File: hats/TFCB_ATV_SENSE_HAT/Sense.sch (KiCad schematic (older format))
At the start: 0 parts

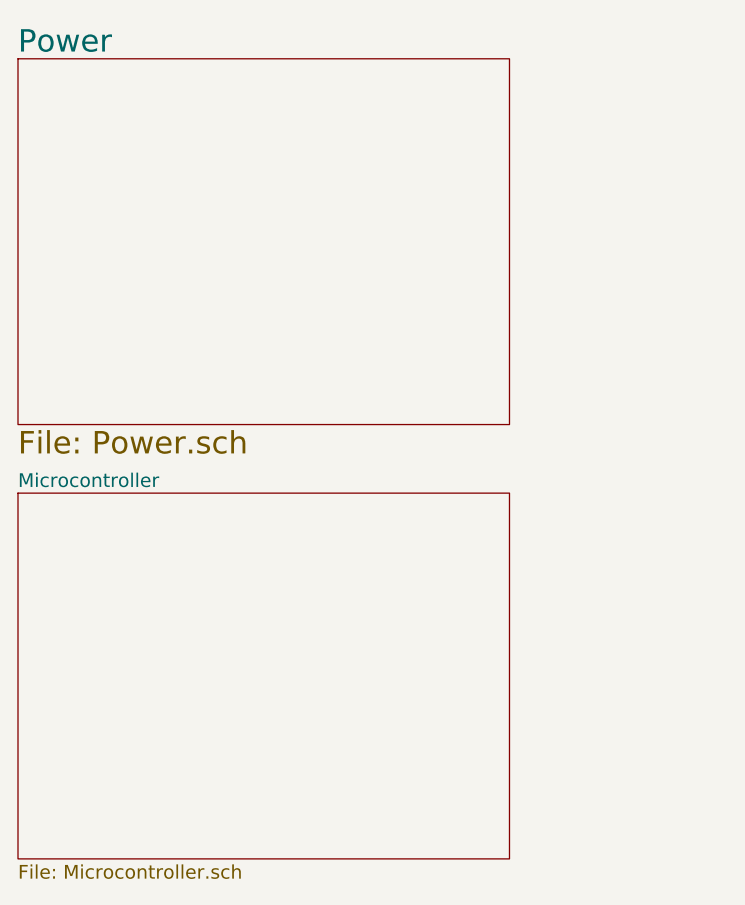
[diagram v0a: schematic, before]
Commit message: Moved power regulators to top side and corrected bad package
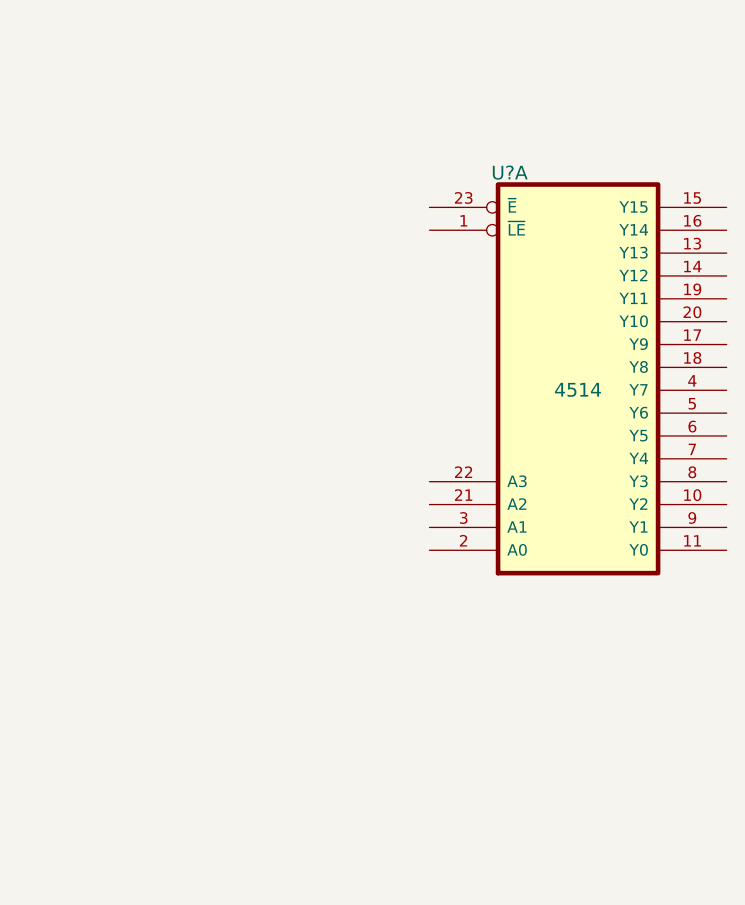
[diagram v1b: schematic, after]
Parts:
- added U?: 4000series-4514, symbol 4000series-4514
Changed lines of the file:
@@
 EESchema Schematic File Version 2
-LIBS:Basics-BJH
-LIBS:buzzer
-LIBS:Connectors-BJH
-LIBS:Devices-BJH
-LIBS:LCD-BJH
-LIBS:Microchip-BJH
-LIBS:Oscillators-BJH
-LIBS:PowerSymbols-BJH
-LIBS:Relays
-LIBS:Transistors-BJH
-LIBS:TFCB-rescue
 LIBS:power
 LIBS:device
@@
 LIBS:contrib
 LIBS:valves
-LIBS:TFCB-cache
+LIBS:Basics-BJH
+LIBS:buzzer
+LIBS:Connectors-BJH
+LIBS:Devices-BJH
+LIBS:LCD-BJH
+LIBS:Microchip-BJH
+LIBS:Oscillators-BJH
+LIBS:PowerSymbols-BJH
+LIBS:Relays
+LIBS:Transistors-BJH
 EELAYER 25 0
 EELAYER END
 $Descr A4 11693 8268
 encoding utf-8
-Sheet 1 3
+Sheet 3 4
 Title ""
 Date ""
 Rev ""
-Comp "hoskins.tech"
+Comp ""
 Comment1 ""
 Comment2 ""
@@
 Comment4 ""
 $EndDescr
-$Sheet
-S 850  900  2150 1600
-U 5507332F
-F0 "Power" 98
-F1 "Power.sch" 98
-$EndSheet
-$Sheet
-S 850  2800 2150 1600
-U 55073CC8
-F0 "Microcontroller" 60
-F1 "Microcontroller.sch" 60
-$EndSheet
+$Comp
+L 4000series-4514 U?
+U 1 1 55E70441
+P 3300 2350
+F 0 "U?" H 3000 3300 60  0000 C CNN
+F 1 "4000series-4514" V 3300 2300 60  0001 C CNN
+F 2 "" H 3500 2300 60  0000 C CNN
+F 3 "" H 3500 2300 60  0000 C CNN
+F 4 "4514" H 3300 2350 60  0000 C CNN "Device"
+	1    3300 2350
+	1    0    0    -1
+$EndComp
 $EndSCHEMATC
